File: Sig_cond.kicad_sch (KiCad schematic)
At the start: 81 parts, among them U401 TSV912IDT, U402 TSV912IDT, U403 TSV912IDT

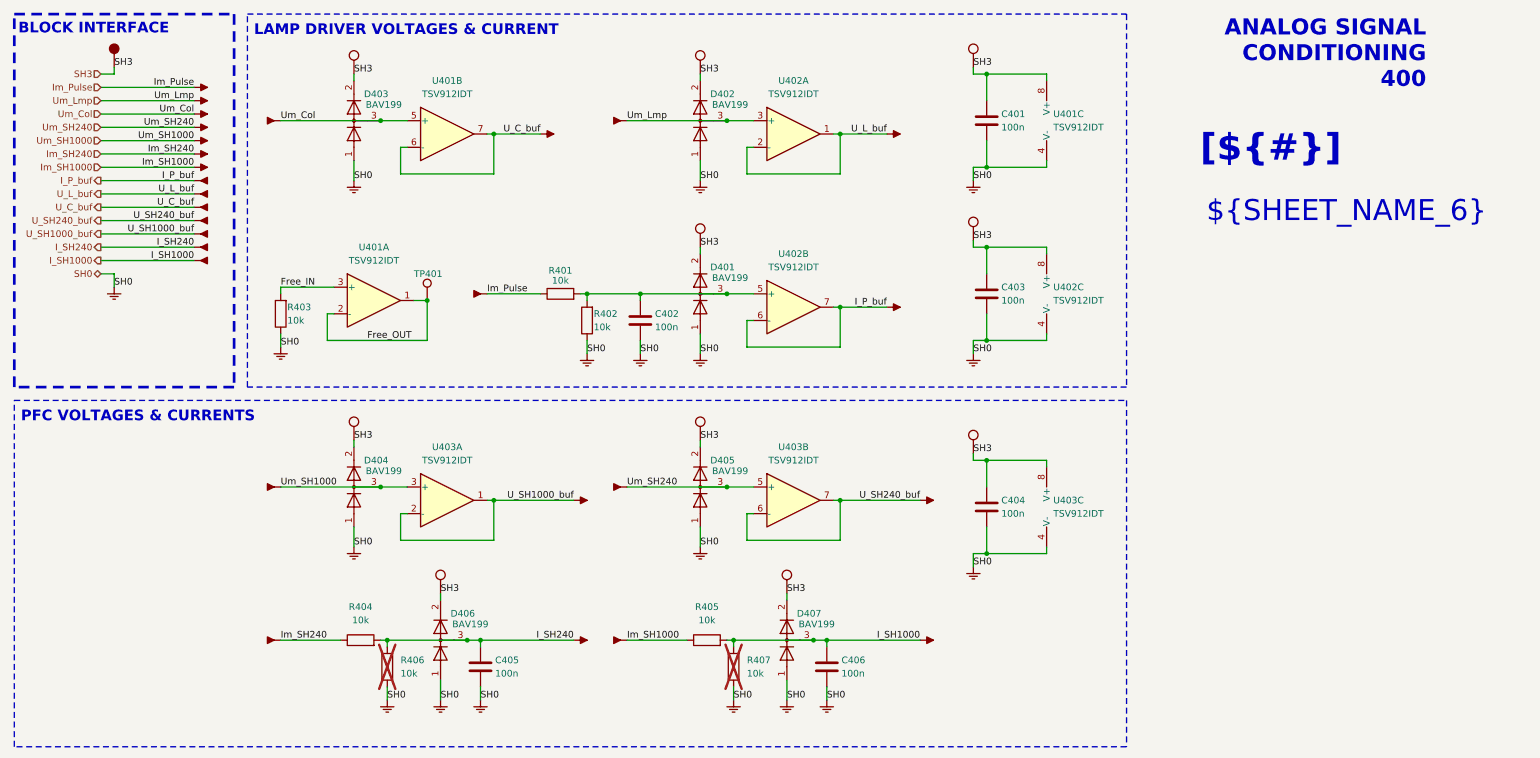
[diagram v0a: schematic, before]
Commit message: Reworked sheet titles
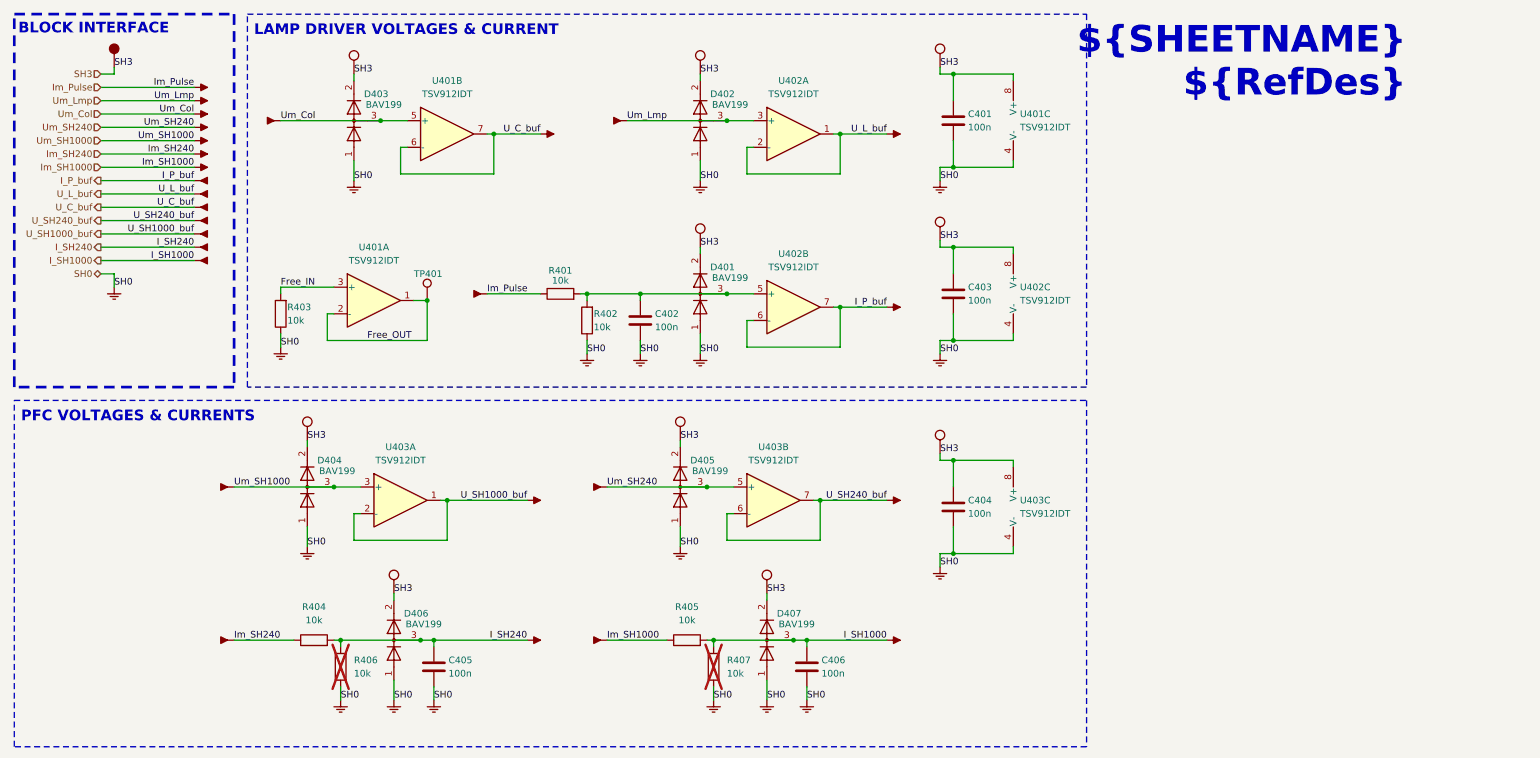
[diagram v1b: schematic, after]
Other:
- note removed: "${SHEET_NAME_6}"
- note removed: "ANALOG SIGNAL CONDITIONING 400"
- title: (none) -> ${SHEETNAME}
- moved on the sheet: C401, C403, C404, C405, C406, D404, D405, D406, D407, R404, R405, R406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

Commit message: Added PCB
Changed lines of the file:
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@@
 	(title_block
 		(title "${SHEETNAME}")
-		(date "2025-01-12")
+		(date "2025-07-04")
 	)
 	(rectangle
@@
 		(at 208.28 15.24 0)
 		(size 73.66 15.24)
-		(margins 2.54 1.27 2.54 1.27)
+		(margins 1.27 1.27 1.27 1.27)
 		(stroke
 			(width -0.0001)
@@
 	)
 	(symbol
-		(lib_name "Cosmetic_PWR_4")
 		(lib_id "personal:Cosmetic_PWR")
 		(at 190.5 97.79 0)
@@
 			)
 		)
-		(property "Description" ""
+		(property "Description" "Local power symbol (sink), cosmetic use only"
 			(at 190.5 97.79 0)
 			(effects
@@
 	)
 	(symbol
-		(lib_name "Cosmetic_PWR_4")
 		(lib_id "personal:Cosmetic_PWR")
 		(at 190.5 24.13 0)
@@
 			)
 		)
-		(property "Description" ""
+		(property "Description" "Local power symbol (sink), cosmetic use only"
 			(at 190.5 24.13 0)
 			(effects
@@
 	)
 	(symbol
-		(lib_name "Cosmetic_PWR_4")
 		(lib_id "personal:Cosmetic_PWR")
 		(at 78.74 25.4 0)
@@
 			)
 		)
-		(property "Description" ""
+		(property "Description" "Local power symbol (sink), cosmetic use only"
 			(at 78.74 25.4 0)
 			(effects
@@
 	)
 	(symbol
-		(lib_name "Cosmetic_PWR_4")
 		(lib_id "personal:Cosmetic_PWR")
 		(at 144.78 58.42 0)
@@
 			)
 		)
-		(property "Description" ""
+		(property "Description" "Local power symbol (sink), cosmetic use only"
 			(at 144.78 58.42 0)
 			(effects
@@
 	)
 	(symbol
-		(lib_name "Cosmetic_PWR_4")
 		(lib_id "personal:Cosmetic_PWR")
 		(at 144.78 25.4 0)
@@
 			)
 		)
-		(property "Description" ""
+		(property "Description" "Local power symbol (sink), cosmetic use only"
 			(at 144.78 25.4 0)
 			(effects
@@
 	)
 	(symbol
-		(lib_name "Cosmetic_PWR_4")
 		(lib_id "personal:Cosmetic_PWR")
 		(at 86.36 124.46 0)
@@
 			)
 		)
-		(property "Description" ""
+		(property "Description" "Local power symbol (sink), cosmetic use only"
 			(at 86.36 124.46 0)
 			(effects
@@
 			)
 		)
-		(property "Description" ""
+		(property "Description" "Local power symbol (source), cosmetic use only"
 			(at 33.02 24.13 0)
 			(effects
@@
 	)
 	(symbol
-		(lib_name "Cosmetic_PWR_4")
 		(lib_id "personal:Cosmetic_PWR")
 		(at 69.85 95.25 0)
@@
 			)
 		)
-		(property "Description" ""
+		(property "Description" "Local power symbol (sink), cosmetic use only"
 			(at 69.85 95.25 0)
 			(effects
@@
 	)
 	(symbol
-		(lib_name "Cosmetic_PWR_4")
 		(lib_id "personal:Cosmetic_PWR")
 		(at 190.5 57.15 0)
@@
 			)
 		)
-		(property "Description" ""
+		(property "Description" "Local power symbol (sink), cosmetic use only"
 			(at 190.5 57.15 0)
 			(effects
@@
 	)
 	(symbol
-		(lib_name "Cosmetic_PWR_4")
 		(lib_id "personal:Cosmetic_PWR")
 		(at 157.48 124.46 0)
@@
 			)
 		)
-		(property "Description" ""
+		(property "Description" "Local power symbol (sink), cosmetic use only"
 			(at 157.48 124.46 0)
 			(effects
@@
 	)
 	(symbol
-		(lib_name "Cosmetic_PWR_4")
 		(lib_id "personal:Cosmetic_PWR")
 		(at 140.97 95.25 0)
@@
 			)
 		)
-		(property "Description" ""
+		(property "Description" "Local power symbol (sink), cosmetic use only"
 			(at 140.97 95.25 0)
 			(effects

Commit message: updating BOM info
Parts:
- C401, C402, C403, C404, C405, C406: Manufacturer (none) -> CCTC; Manufacturer Part Number (none) -> TCC0603X7R104K500CT
- D401, D402, D403, D404, D405, D406, D407: Manufacturer (none) -> onsemi; Manufacturer Part Number (none) -> BAV199LT1G
- R401, R402, R403, R404, R405: Manufacturer (none) -> Generic
- TP401: now left out of the parts list
- U401, U402, U403: Manufacturer (none) -> ST; Manufacturer Part Number (none) -> TSV912IDT

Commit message: Sch update in progress
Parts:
- removed C403: 100n, Capacitor_SMD:C_0603_1608Metric_Pad1.08x0.95mm_HandSolder, symbol Device:C
- removed D404: BAV199, Package_TO_SOT_SMD:SOT-23, symbol Diode:BAV99
- removed P451, P598: ~, symbol personal:Cosmetic_OUT
- removed P581, P594: ~, symbol personal:Cosmetic_PWR
- removed P816, P822, P823: ~, symbol personal:Cosmetic_GND
- removed P865, P876: ~, symbol personal:Cosmetic_IN
- removed R403: 10k, Resistor_SMD:R_0603_1608Metric_Pad0.98x0.95mm_HandSolder, symbol Device:R
- removed TP401: TestPoint, TestPoint:TestPoint_THTPad_D1.0mm_Drill0.5mm, symbol Connector:TestPoint
- removed U402: TSV912IDT, Package_SO:SOIC-8_3.9x4.9mm_P1.27mm, symbol Amplifier_Operational:TSV912IDT
- added P306: ~, symbol personal:Cosmetic_IN
- C402: value 100n -> 4n7
- R401, R402: value 10k -> 220
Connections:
- net I_P_buf is gone; now on net Mon_IL_prot: P449.1, P872.1
- net U_L_buf is gone; now on net Mon_S1k_buf: P588.1, P873.1
- net Um_Lmp is gone; now on net Mon_S1k: D402.3 (K), P446.1, P869.1
- net Mon_IL_prot: now reaches C402.1, D401.3 (K), R401.2, R402.2
- net Free_IN renamed Mon_S1k
- net Free_OUT renamed Mon_S1k_buf
- net I_SH1000 renamed I_S1k
- net Im_Pulse renamed Mon_IL
- net Im_SH1000 renamed Im_S1k
- net U_C_buf renamed Mon_LMP_buf
- net U_SH1000_buf: no longer names the net of U403.1
- net U_SH1000_buf: no longer U403.2 (-)
- net Um_Col renamed Mon_LMP
- net Um_SH1000: no longer names the net of U403.3 (+)
- no-connect marks 0 -> 3
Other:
- moved on the sheet: C401, C402, D401, R401, R402, U401A, U401C

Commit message: Sch update in progres
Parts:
- removed C404, C405, C406: 100n, Capacitor_SMD:C_0603_1608Metric_Pad1.08x0.95mm_HandSolder, symbol Device:C
- removed D405, D406, D407: BAV199, Package_TO_SOT_SMD:SOT-23, symbol Diode:BAV99
- removed P306, P866, P867, P868, P875, P877, P878: ~, symbol personal:Cosmetic_IN
- removed P450, P452, P574, P599, P606, P608: ~, symbol personal:Cosmetic_OUT
- removed P593, P595, P603, P604: ~, symbol personal:Cosmetic_PWR
- removed P824, P825, P826, P827, P828, P829, P830, P831: ~, symbol personal:Cosmetic_GND
- removed R404, R405, R406, R407: 10k, Resistor_SMD:R_0603_1608Metric_Pad0.98x0.95mm_HandSolder, symbol Device:R
- removed U403: TSV912IDT, Package_SO:SOIC-8_3.9x4.9mm_P1.27mm, symbol Amplifier_Operational:TSV912IDT
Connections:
- no-connect marks 3 -> 0
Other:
- note removed: "PFC VOLTAGES & CURRENTS"

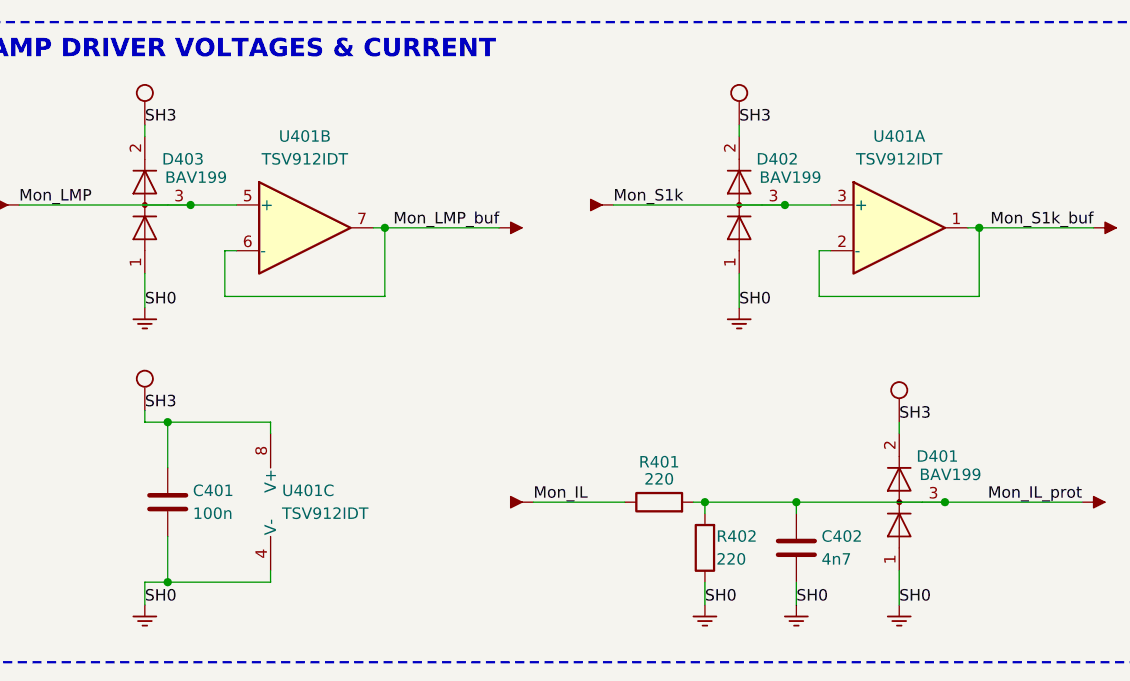
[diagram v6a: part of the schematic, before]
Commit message: Reannotated, silk done, missing some 3D models
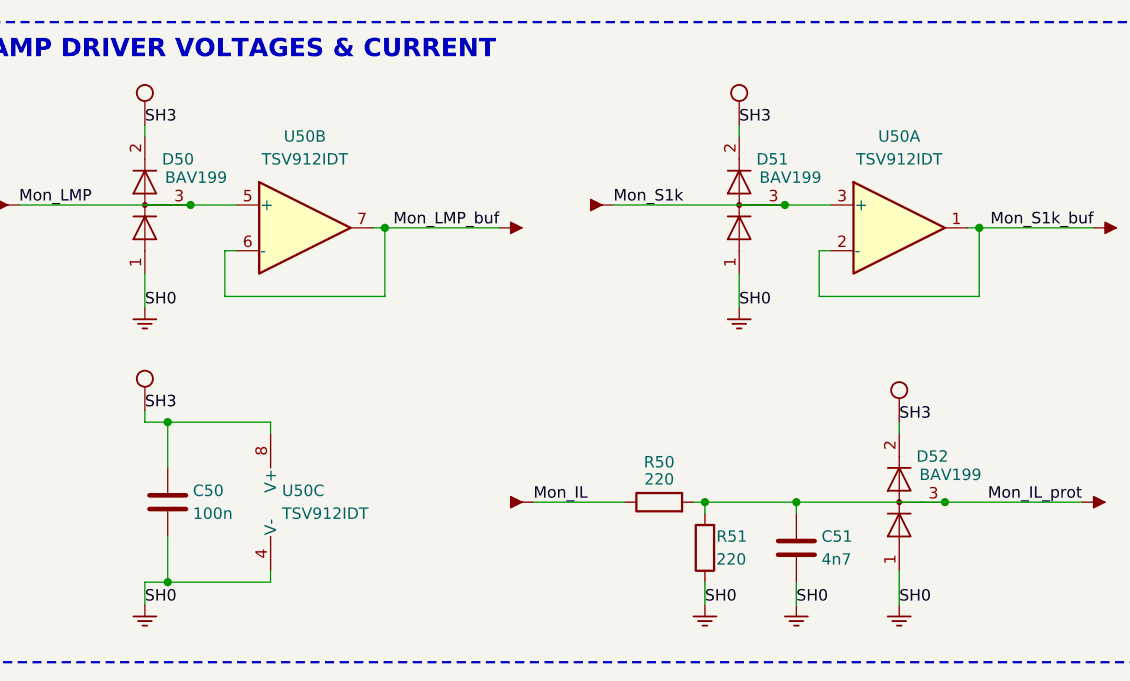
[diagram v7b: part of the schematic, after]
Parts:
- renumbered C401 to C50, C402 to C51, D403 to D50, D402 to D51, D401 to D52, P796 to P109, P584 to P110, P583 to P111, P445 to P112, P446 to P113, P448 to P114, P871 to P115, P869 to P116, P872 to P117, P589 to P118, P588 to P119, P873 to P120, P874 to P121, P585 to P122, P815 to P123, P818 to P124, P442 to P125, P443 to P126, P870 to P127, P449 to P128, P817 to P129, P819 to P130, P820 to P137, P821 to P138, R401 to R50, R402 to R51, U401 to U50

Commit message: Changed to checked, updated fab pdf yaml
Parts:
- C50, C51: MAN (none) -> Generic; Manufacturer CCTC -> Generic; Manufacturer Part Number TCC0603X7R104K500CT -> (none)
- D50, D51, D52: MAN (none) -> onsemi; MPN (none) -> BAV199LT1G
- R50, R51: MAN (none) -> Generic
- U50: MAN (none) -> ST; MPN (none) -> TSV912IDT
